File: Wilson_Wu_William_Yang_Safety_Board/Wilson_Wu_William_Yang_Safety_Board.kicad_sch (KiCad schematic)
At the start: 40 parts, among them J1 22035035, J4 M22-7130442, J8 430450200, U1 STM32, U11 LMV331IDBVR, U2 MCP2562-E_P, U3 10kohm, U4 SN74HCS21QPWRQ1

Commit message: layout
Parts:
- added octocoupler_tp1: V_DIVIDED, TestPoint:TestPoint_Pad_D1.0mm, symbol Connector:TestPoint
- renumbered TP33 to CAN_NEG_TP1, TP32 to CAN_POS_TP1, TP10 to IgnitionSignal_TP1, TP15 to RXD_TP1, TP14 to TXD_TP1, TP9 to hsensor_output_tp1, TP1 to mosfet_conn_tp1
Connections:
- net optocoupler-output: now also octocoupler_tp1.1
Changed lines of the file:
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@@
 	)
 	(junction
+		(at 35.56 189.23)
+		(diameter 0)
+		(color 0 0 0 0)
+	)
+	(junction
 		(at 270.51 132.08)
 		(diameter 0)
@@
 	(wire
 		(pts
-			(xy 34.29 189.23) (xy 36.83 189.23)
+			(xy 34.29 189.23) (xy 35.56 189.23)
 		)
 		(stroke
@@
 	(wire
 		(pts
+			(xy 35.56 189.23) (xy 36.83 189.23)
+		)
+		(stroke
+			(width 0)
+			(type default)
+		)
+	)
+	(wire
+		(pts
 			(xy 196.85 124.46) (xy 196.85 129.54)
 		)
@@
 		(dnp no)
 		(fields_autoplaced yes)
-		(property "Reference" "TP15"
+		(property "Reference" "RXD_TP1"
 			(at 114.3 136.6519 0)
 			(effects
@@
 			(project "Wilson_Wu_William_Yang_Safety_Board"
 				(path "/fa857c32-0741-4b91-b122-1a57686bb514"
-					(reference "TP15")
+					(reference "RXD_TP1")
 					(unit 1)
 				)
@@
 		(dnp no)
 		(fields_autoplaced yes)
-		(property "Reference" "TP14"
+		(property "Reference" "TXD_TP1"
 			(at 114.3 122.4279 0)
 			(effects
@@
 			(project "Wilson_Wu_William_Yang_Safety_Board"
 				(path "/fa857c32-0741-4b91-b122-1a57686bb514"
-					(reference "TP14")
+					(reference "TXD_TP1")
 					(unit 1)
 				)
@@
 		(on_board yes)
 		(dnp no)
-		(property "Reference" "TP33"
+		(property "Reference" "CAN_NEG_TP1"
 			(at 265.684 113.284 0)
 			(effects
@@
 			(project "Wilson_Wu_William_Yang_Safety_Board"
 				(path "/fa857c32-0741-4b91-b122-1a57686bb514"
-					(reference "TP33")
+					(reference "CAN_NEG_TP1")
 					(unit 1)
 				)
@@
 		(on_board yes)
 		(dnp no)
-		(property "Reference" "TP10"
+		(property "Reference" "IgnitionSignal_TP1"
 			(at 33.782 160.782 0)
 			(effects
@@
 			(project "Wilson_Wu_William_Yang_Safety_Board"
 				(path "/fa857c32-0741-4b91-b122-1a57686bb514"
-					(reference "TP10")
+					(reference "IgnitionSignal_TP1")
 					(unit 1)
 				)
@@
 		(on_board yes)
 		(dnp no)
-		(property "Reference" "TP32"
+		(property "Reference" "CAN_POS_TP1"
 			(at 263.144 134.366 0)
 			(effects
@@
 			(project "Wilson_Wu_William_Yang_Safety_Board"
 				(path "/fa857c32-0741-4b91-b122-1a57686bb514"
-					(reference "TP32")
+					(reference "CAN_POS_TP1")
 					(unit 1)
 				)
@@
 		(dnp no)
 		(fields_autoplaced yes)
-		(property "Reference" "TP9"
-			(at 247.65 32.2581 0)
+		(property "Reference" "hsensor_output_tp1"
+			(at 252.73 29.7179 0)
 			(effects
 				(font
 					(size 1.27 1.27)
 				)
-				(justify right)
+				(justify left)
 			)
 		)
 		(property "Value" "TestPoint"
-			(at 247.65 29.7181 0)
+			(at 252.73 32.2579 0)
 			(effects
 				(font
 					(size 1.27 1.27)
 				)
-				(justify right)
+				(justify left)
 			)
 		)
@@
 			(project "Wilson_Wu_William_Yang_Safety_Board"
 				(path "/fa857c32-0741-4b91-b122-1a57686bb514"
-					(reference "TP9")
+					(reference "hsensor_output_tp1")
 					(unit 1)
 				)
@@
 	)
 	(symbol
+		(lib_id "Connector:TestPoint")
+		(at 35.56 189.23 180)
+		(unit 1)
+		(exclude_from_sim no)
+		(in_bom yes)
+		(on_board yes)
+		(dnp no)
+		(fields_autoplaced yes)
+		(property "Reference" "octocoupler_tp1"
+			(at 38.1 192.5319 0)
+			(effects
+				(font
+					(size 1.27 1.27)
+				)
+				(justify right)
+			)
+		)
+		(property "Value" "V_DIVIDED"
+			(at 33.02 191.2621 0)
+			(effects
+				(font
+					(size 1.27 1.27)
+				)
+				(justify left)
+				(hide yes)
+			)
+		)
+		(property "Footprint" "TestPoint:TestPoint_Pad_D1.0mm"
+			(at 30.48 189.23 0)
+			(effects
+				(font
+					(size 1.27 1.27)
+				)
+				(hide yes)
+			)
+		)
+		(property "Datasheet" "~"
+			(at 30.48 189.23 0)
+			(effects
+				(font
+					(size 1.27 1.27)
+				)
+				(hide yes)
+			)
+		)
+		(property "Description" "test point"
+			(at 35.56 189.23 0)
+			(effects
+				(font
+					(size 1.27 1.27)
+				)
+				(hide yes)
+			)
+		)
+		(pin "1"
+		)
+		(instances
+			(project "Wilson_Wu_William_Yang_Safety_Board"
+				(path "/fa857c32-0741-4b91-b122-1a57686bb514"
+					(reference "octocoupler_tp1")
+					(unit 1)
+				)
+			)
+		)
+	)
+	(symbol
 		(lib_id "power:GND")
 		(at 24.13 115.57 0)
@@
 		(on_board yes)
 		(dnp no)
-		(property "Reference" "TP1"
+		(property "Reference" "mosfet_conn_tp1"
 			(at 255.27 51.3081 0)
 			(effects
@@
 			(project "Wilson_Wu_William_Yang_Safety_Board"
 				(path "/fa857c32-0741-4b91-b122-1a57686bb514"
-					(reference "TP1")
+					(reference "mosfet_conn_tp1")
 					(unit 1)
 				)

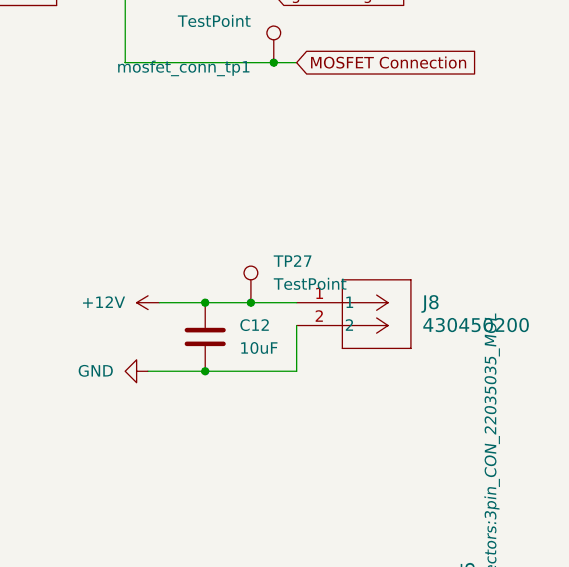
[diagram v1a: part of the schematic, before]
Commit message: layout fixes
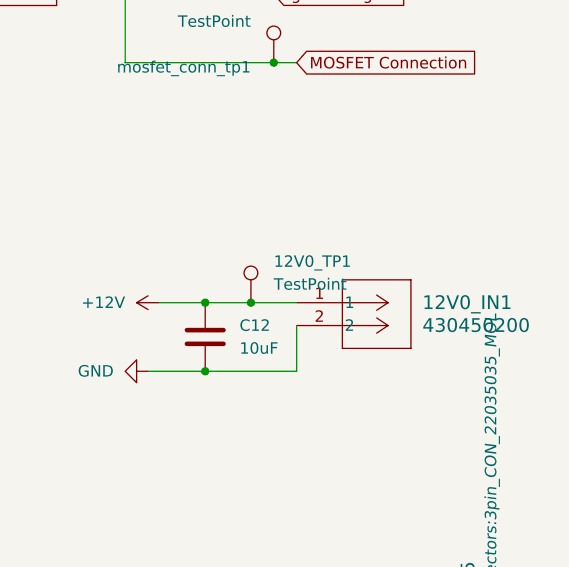
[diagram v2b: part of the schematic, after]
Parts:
- renumbered J8 to 12V0_IN1, TP27 to 12V0_TP1
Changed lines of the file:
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@@
 		(dnp no)
 		(fields_autoplaced yes)
-		(property "Reference" "J8"
+		(property "Reference" "12V0_IN1"
 			(at 274.32 77.4699 0)
 			(effects
@@
 			(project ""
 				(path "/fa857c32-0741-4b91-b122-1a57686bb514"
-					(reference "J8")
+					(reference "12V0_IN1")
 					(unit 1)
 				)
@@
 		(dnp no)
 		(fields_autoplaced yes)
-		(property "Reference" "TP27"
+		(property "Reference" "12V0_TP1"
 			(at 257.81 72.8979 0)
 			(effects
@@
 			(project "Wilson_Wu_William_Yang_Safety_Board"
 				(path "/fa857c32-0741-4b91-b122-1a57686bb514"
-					(reference "TP27")
+					(reference "12V0_TP1")
 					(unit 1)
 				)

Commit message: update
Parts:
- added Q5: IRLML6344TRPBF, Test:TRANS_IRLML6344TRPBF, symbol IRLML6344TRPBF:IRLML6344TRPBF
- added R_7: 0, Resistor_SMD:R_0805_2012Metric, symbol Device:R_US
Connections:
- net GND: now also Q5.2
- net at U1.35 (PC2): now also Q5.1
- new net: Q5.3, R_7.2
- new net drain: R_7.1
- no-connect marks 52 -> 53

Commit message: resistors
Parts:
- added R10: 100, Resistor_SMD:R_0805_2012Metric, symbol Device:R_US
- added R15: 100k, Resistor_SMD:R_0805_2012Metric, symbol Device:R_US
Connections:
- net GND: now also R15.2
- net at Q5.1: now also R10.2, R15.1; no longer U1.35 (PC2)
- new net: R10.1, U1.35 (PC2)
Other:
- moved on the sheet: R_7
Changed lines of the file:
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@@
 	)
 	(junction
+		(at 6.35 170.18)
+		(diameter 0)
+		(color 0 0 0 0)
+	)
+	(junction
 		(at 101.6 166.37)
 		(diameter 0)
@@
 	)
 	(junction
+		(at 13.97 181.61)
+		(diameter 0)
+		(color 0 0 0 0)
+	)
+	(junction
 		(at 34.29 143.51)
 		(diameter 0)
@@
 	(wire
 		(pts
+			(xy 11.43 181.61) (xy 13.97 181.61)
+		)
+		(stroke
+			(width 0)
+			(type default)
+		)
+	)
+	(wire
+		(pts
+			(xy -5.08 189.23) (xy 6.35 189.23)
+		)
+		(stroke
+			(width 0)
+			(type default)
+		)
+	)
+	(wire
+		(pts
 			(xy 255.27 77.47) (xy 260.35 77.47)
 		)
@@
 	(wire
 		(pts
+			(xy 25.4 181.61) (xy 36.83 181.61)
+		)
+		(stroke
+			(width 0)
+			(type default)
+		)
+	)
+	(wire
+		(pts
 			(xy 25.4 163.83) (xy 26.67 163.83)
 		)
@@
 	(wire
 		(pts
-			(xy -3.81 189.23) (xy -2.54 189.23)
+			(xy -13.97 189.23) (xy -12.7 189.23)
 		)
 		(stroke
@@
 	(wire
 		(pts
+			(xy 13.97 181.61) (xy 17.78 181.61)
+		)
+		(stroke
+			(width 0)
+			(type default)
+		)
+	)
+	(wire
+		(pts
 			(xy 184.15 44.45) (xy 184.15 34.29)
 		)
@@
 	(wire
 		(pts
+			(xy 13.97 170.18) (xy 6.35 170.18)
+		)
+		(stroke
+			(width 0)
+			(type default)
+		)
+	)
+	(wire
+		(pts
 			(xy 95.25 83.82) (xy 93.98 83.82)
 		)
@@
 	(wire
 		(pts
+			(xy 6.35 170.18) (xy 6.35 179.07)
+		)
+		(stroke
+			(width 0)
+			(type default)
+		)
+	)
+	(wire
+		(pts
 			(xy 111.76 133.35) (xy 111.76 134.62)
 		)
@@
 	(wire
 		(pts
-			(xy 6.35 189.23) (xy 5.08 189.23)
+			(xy 13.97 180.34) (xy 13.97 181.61)
 		)
 		(stroke
@@
 	(wire
 		(pts
-			(xy 250.19 34.29) (xy 255.27 34.29)
+			(xy 13.97 172.72) (xy 13.97 170.18)
 		)
 		(stroke
@@
 	(wire
 		(pts
-			(xy 175.26 93.98) (xy 175.26 91.44)
+			(xy 250.19 34.29) (xy 255.27 34.29)
 		)
 		(stroke
@@
 	(wire
 		(pts
-			(xy 99.06 130.81) (xy 111.76 130.81)
+			(xy 175.26 93.98) (xy 175.26 91.44)
 		)
 		(stroke
@@
 	(wire
 		(pts
-			(xy 193.04 124.46) (xy 196.85 124.46)
+			(xy 99.06 130.81) (xy 111.76 130.81)
 		)
 		(stroke
@@
 	(wire
 		(pts
-			(xy 181.61 30.48) (xy 200.66 30.48)
+			(xy 193.04 124.46) (xy 196.85 124.46)
 		)
 		(stroke
@@
 	(wire
 		(pts
-			(xy 260.35 80.01) (xy 260.35 85.09)
+			(xy 181.61 30.48) (xy 200.66 30.48)
 		)
 		(stroke
@@
 	(wire
 		(pts
-			(xy 11.43 181.61) (xy 36.83 181.61)
+			(xy 260.35 80.01) (xy 260.35 85.09)
 		)
 		(stroke
@@
 	(wire
 		(pts
-			(xy 6.35 179.07) (xy 6.35 175.26)
+			(xy 6.35 167.64) (xy 6.35 170.18)
 		)
 		(stroke
@@
 	(global_label "drain"
 		(shape input)
-		(at -3.81 189.23 180)
+		(at -13.97 189.23 180)
 		(fields_autoplaced yes)
 		(effects
@@
 		)
 		(property "Intersheetrefs" "${INTERSHEET_REFS}"
-			(at -11.6332 189.23 0)
+			(at -21.7932 189.23 0)
 			(effects
 				(font
@@
 	)
 	(symbol
+		(lib_id "Device:R_US")
+		(at 13.97 176.53 180)
+		(unit 1)
+		(exclude_from_sim no)
+		(in_bom yes)
+		(on_board yes)
+		(dnp no)
+		(property "Reference" "R15"
+			(at 14.986 175.26 0)
+			(effects
+				(font
+					(size 1.27 1.27)
+				)
+				(justify right)
+			)
+		)
+		(property "Value" "100k"
+			(at 14.986 177.8 0)
+			(effects
+				(font
+					(size 1.27 1.27)
+				)
+				(justify right)
+			)
+		)
+		(property "Footprint" "Resistor_SMD:R_0805_2012Metric"
+			(at 12.954 176.276 90)
+			(effects
+				(font
+					(size 1.27 1.27)
+				)
+				(hide yes)
+			)
+		)
+		(property "Datasheet" "~"
+			(at 13.97 176.53 0)
+			(effects
+				(font
+					(size 1.27 1.27)
+				)
+				(hide yes)
+			)
+		)
+		(property "Description" "Resistor, US symbol"
+			(at 13.97 176.53 0)
+			(effects
+				(font
+					(size 1.27 1.27)
+				)
+				(hide yes)
+			)
+		)
+		(pin "2"
+		)
+		(pin "1"
+		)
+		(instances
+			(project "Wilson_Wu_William_Yang_Safety_Board"
+				(path "/fa857c32-0741-4b91-b122-1a57686bb514"
+					(reference "R15")
+					(unit 1)
+				)
+			)
+		)
+	)
+	(symbol
 		(lib_id "power:+3.3V")
 		(at 93.98 83.82 90)
@@
 	(symbol
 		(lib_id "power:GND")
-		(at 6.35 175.26 180)
+		(at 6.35 167.64 180)
 		(unit 1)
 		(exclude_from_sim no)
@@
 		(fields_autoplaced yes)
 		(property "Reference" "#PWR065"
-			(at 6.35 168.91 0)
+			(at 6.35 161.29 0)
 			(effects
 				(font
@@
 		)
 		(property "Value" "GND"
-			(at 6.35 170.18 0)
+			(at 6.35 162.56 0)
 			(effects
 				(font
@@
 		)
 		(property "Footprint" ""
-			(at 6.35 175.26 0)
+			(at 6.35 167.64 0)
 			(effects
 				(font
@@
 		)
 		(property "Datasheet" ""
-			(at 6.35 175.26 0)
+			(at 6.35 167.64 0)
 			(effects
 				(font
@@
 		)
 		(property "Description" "Power symbol creates a global label with name \"GND\" , ground"
-			(at 6.35 175.26 0)
+			(at 6.35 167.64 0)
 			(effects
 				(font
@@
 	(symbol
 		(lib_id "Device:R_US")
+		(at 21.59 181.61 270)
+		(unit 1)
+		(exclude_from_sim no)
+		(in_bom yes)
+		(on_board yes)
+		(dnp no)
+		(property "Reference" "R10"
+			(at 20.32 180.594 0)
+			(effects
+				(font
+					(size 1.27 1.27)
+				)
+				(justify right)
+			)
+		)
+		(property "Value" "100"
+			(at 22.86 180.594 0)
+			(effects
+				(font
+					(size 1.27 1.27)
+				)
+				(justify right)
+			)
+		)
+		(property "Footprint" "Resistor_SMD:R_0805_2012Metric"
+			(at 21.336 182.626 90)
+			(effects
+				(font
+					(size 1.27 1.27)
+				)
+				(hide yes)
+			)
+		)
+		(property "Datasheet" "~"
+			(at 21.59 181.61 0)
+			(effects
+				(font
+					(size 1.27 1.27)
+				)
+				(hide yes)
+			)
+		)
+		(property "Description" "Resistor, US symbol"
+			(at 21.59 181.61 0)
+			(effects
+				(font
+					(size 1.27 1.27)
+				)
+				(hide yes)
+			)
+		)
+		(pin "2"
+		)
+		(pin "1"
+		)
+		(instances
+			(project "Wilson_Wu_William_Yang_Safety_Board"
+				(path "/fa857c32-0741-4b91-b122-1a57686bb514"
+					(reference "R10")
+					(unit 1)
+				)
+			)
+		)
+	)
+	(symbol
+		(lib_id "Device:R_US")
 		(at 99.06 83.82 90)
 		(unit 1)
@@
 	(symbol
 		(lib_id "Device:R_US")
-		(at 1.27 189.23 90)
+		(at -8.89 189.23 90)
 		(unit 1)
 		(exclude_from_sim no)
@@
 		(dnp no)
 		(property "Reference" "R_7"
-			(at 1.27 185.166 90)
+			(at -8.89 185.166 90)
 			(effects
 				(font
@@
 		)
 		(property "Value" "0"
-			(at 1.27 187.198 90)
+			(at -8.89 187.198 90)
 			(effects
 				(font
@@
 		)
 		(property "Footprint" "Resistor_SMD:R_0805_2012Metric"
-			(at 1.524 188.214 90)
+			(at -8.636 188.214 90)
 			(effects
 				(font
@@
 		)
 		(property "Datasheet" "~"
-			(at 1.27 189.23 0)
+			(at -8.89 189.23 0)
 			(effects
 				(font
@@
 		)
 		(property "Description" "Resistor, US symbol"
-			(at 1.27 189.23 0)
+			(at -8.89 189.23 0)
 			(effects
 				(font

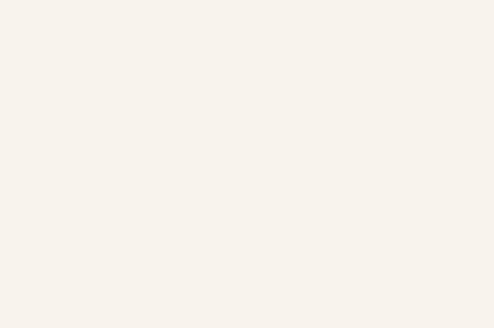
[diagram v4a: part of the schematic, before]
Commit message: updated led positioning
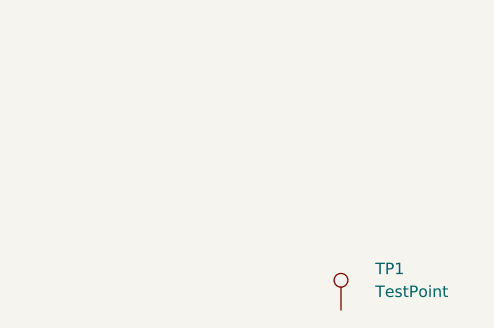
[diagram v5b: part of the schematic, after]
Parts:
- added TP1: TestPoint, SMV_Logo:SEM_logo, symbol Connector:TestPoint
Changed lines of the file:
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@@
+	(symbol
+		(lib_id "Connector:TestPoint")
+		(at 283.21 220.98 0)
+		(unit 1)
+		(exclude_from_sim no)
+		(in_bom yes)
+		(on_board yes)
+		(dnp no)
+		(fields_autoplaced yes)
+		(property "Reference" "TP1"
+			(at 287.02 216.4079 0)
+			(effects
+				(font
+					(size 1.27 1.27)
+				)
+				(justify left)
+			)
+		)
+		(property "Value" "TestPoint"
+			(at 287.02 218.9479 0)
+			(effects
+				(font
+					(size 1.27 1.27)
+				)
+				(justify left)
+			)
+		)
+		(property "Footprint" "SMV_Logo:SEM_logo"
+			(at 288.29 220.98 0)
+			(effects
+				(font
+					(size 1.27 1.27)
+				)
+				(hide yes)
+			)
+		)
+		(property "Datasheet" "~"
+			(at 288.29 220.98 0)
+			(effects
+				(font
+					(size 1.27 1.27)
+				)
+				(hide yes)
+			)
+		)
+		(property "Description" "test point"
+			(at 283.21 220.98 0)
+			(effects
+				(font
+					(size 1.27 1.27)
+				)
+				(hide yes)
+			)
+		)
+		(pin "1"
+		)
+		(instances
+			(project "Wilson_Wu_William_Yang_Safety_Board"
+				(path "/fa857c32-0741-4b91-b122-1a57686bb514"
+					(reference "TP1")
+					(unit 1)
+				)
+			)
+		)
+	)
 	(symbol
 		(lib_id "Connector:TestPoint")

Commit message: led changes
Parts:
- v-dvider-tp1: renamed from TP6; value TestPoint -> v-dvider-tp
- renumbered TP2 to ina_tp1
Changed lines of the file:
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@@
 		(on_board yes)
 		(dnp no)
-		(property "Reference" "TP2"
+		(property "Reference" "ina_tp1"
 			(at 180.086 106.426 0)
 			(effects
@@
 			(project "Wilson_Wu_William_Yang_Safety_Board"
 				(path "/fa857c32-0741-4b91-b122-1a57686bb514"
-					(reference "TP2")
+					(reference "ina_tp1")
 					(unit 1)
 				)
@@
 		(dnp no)
 		(fields_autoplaced yes)
-		(property "Reference" "TP6"
-			(at 104.648 88.9 90)
-			(effects
-				(font
-					(size 1.27 1.27)
-				)
-			)
-		)
-		(property "Value" "TestPoint"
+		(property "Reference" "v-dvider-tp1"
 			(at 104.648 91.44 90)
 			(effects
@@
 					(size 1.27 1.27)
 				)
+			)
+		)
+		(property "Value" "v-dvider-tp"
+			(at 104.648 91.44 90)
+			(effects
+				(font
+					(size 1.27 1.27)
+				)
+				(hide yes)
 			)
 		)
@@
 			(project "Wilson_Wu_William_Yang_Safety_Board"
 				(path "/fa857c32-0741-4b91-b122-1a57686bb514"
-					(reference "TP6")
-					(unit 1)
-				)
+					(reference "v-dvider-tp1")
+					(unit 1)
+				)

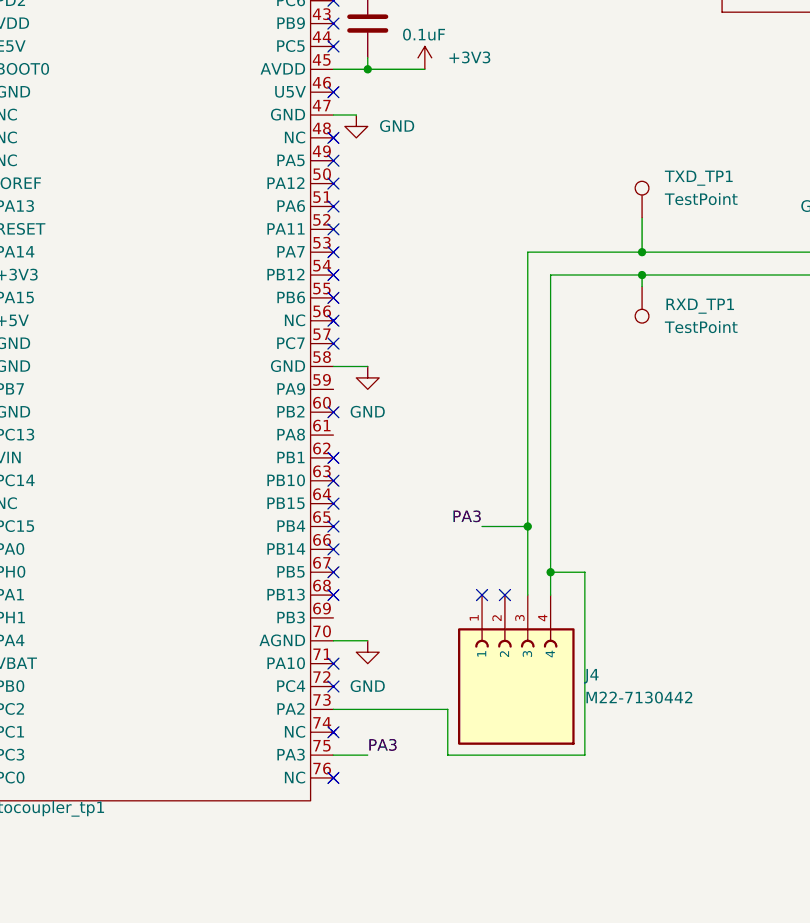
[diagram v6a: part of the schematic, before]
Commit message: switch pins for can tx and rx
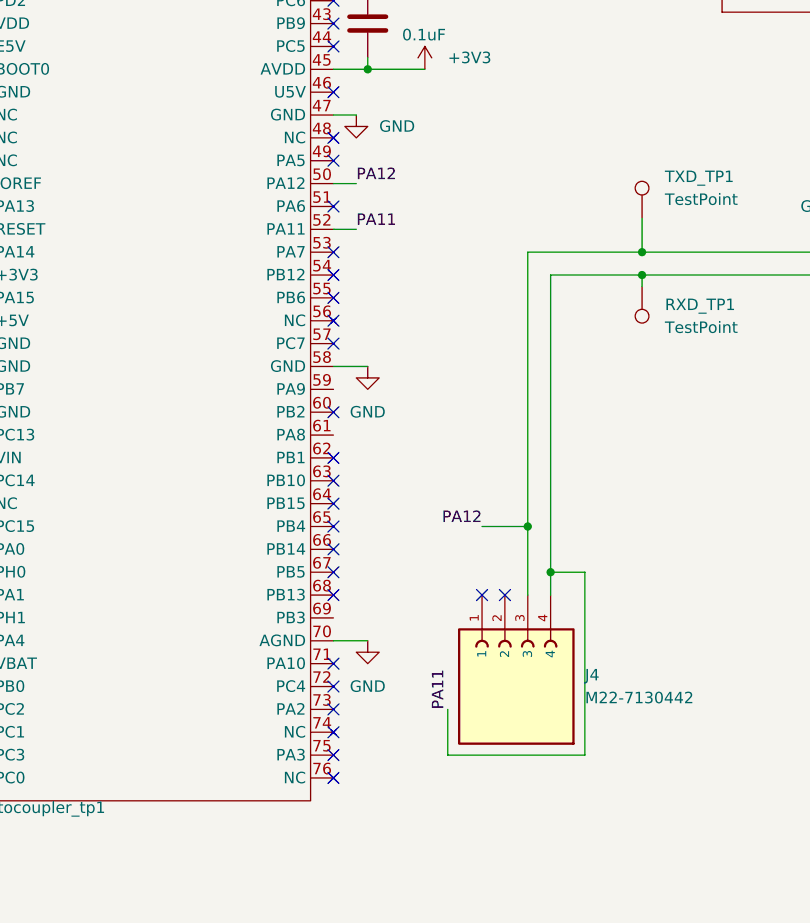
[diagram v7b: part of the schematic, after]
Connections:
- net PA11: now reaches J4.4, RXD_TP1.1, U2.4 (RXD)
- net PA11: now also U1.52 (PA11); no longer U1.73 (PA2)
- net PA12: now reaches U1.50 (PA12)
- net PA12: now also J4.3, TXD_TP1.1, U2.1 (TXD)
- removed net PA3: J4.3, TXD_TP1.1, U1.75 (PA3), U2.1 (TXD)
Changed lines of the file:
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@@
+	)
+	(no_connect
+		(at 77.47 181.61)
 	)
 	(no_connect
@@
 	)
 	(no_connect
+		(at 77.47 186.69)
+	)
+	(no_connect
 		(at 77.47 125.73)
 	)
@@
 	)
 	(no_connect
-		(at 77.47 128.27)
-	)
-	(no_connect
 		(at 36.83 110.49)
 	)
@@
 	)
 	(no_connect
-		(at 77.47 123.19)
-	)
-	(no_connect
 		(at 77.47 179.07)
 	)
@@
 	(wire
 		(pts
-			(xy 77.47 186.69) (xy 81.28 186.69)
-		)
-		(stroke
-			(width 0)
-			(type default)
-		)
-	)
-	(wire
-		(pts
 			(xy 262.89 17.78) (xy 262.89 19.05)
 		)
@@
 	(wire
 		(pts
-			(xy 90.17 181.61) (xy 77.47 181.61)
-		)
-		(stroke
-			(width 0)
-			(type default)
-		)
-	)
-	(wire
-		(pts
 			(xy 173.99 138.43) (xy 177.8 138.43)
 		)
@@
 	(wire
 		(pts
+			(xy 80.01 123.19) (xy 77.47 123.19)
+		)
+		(stroke
+			(width 0)
+			(type default)
+		)
+	)
+	(wire
+		(pts
 			(xy 101.6 168.91) (xy 101.6 166.37)
 		)
@@
 	(wire
 		(pts
+			(xy 80.01 128.27) (xy 77.47 128.27)
+		)
+		(stroke
+			(width 0)
+			(type default)
+		)
+	)
+	(wire
+		(pts
 			(xy 262.89 26.67) (xy 262.89 29.21)
 		)
@@
 		)
 	)
-	(label "PA3"
+	(label "PA12"
 		(at 93.98 161.29 180)
 		(effects
@@
 		)
 	)
-	(label "PA3"
-		(at 81.28 186.69 0)
+	(label "PA11"
+		(at 90.17 181.61 90)
 		(effects
 			(font
+				(size 1.27 1.27)
+			)
+			(justify left bottom)
+		)
+	)
+	(label "PA12"
+		(at 80.01 123.19 0)
+		(effects
+			(font
+				(size 1.27 1.27)
+			)
+			(justify left bottom)
+		)
+	)
+	(label "PA11"
+		(at 80.01 128.27 0)
+		(effects
+			(font
